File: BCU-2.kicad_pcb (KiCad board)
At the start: 2 copper layers, 91.9 x 68 mm, 70 parts, among them J1 Conn_01x12_Male, J2 Conn_01x04_Male, J3 Screw_Terminal_01x04, J4 Screw_Terminal_01x04, Q1 2N7002, Q2 NTF6P02, Q3 2N7002, Q4 2N7002, Q5 NTF6P02, Q6 2N7002, U1 PCF8574, U2 INA219xID, U3 INA219xID, U4 HCPL-181, U5 HCPL-181, U6 HCPL-181, U7 HCPL-181, U8 HCPL-181, U9 HCPL-181

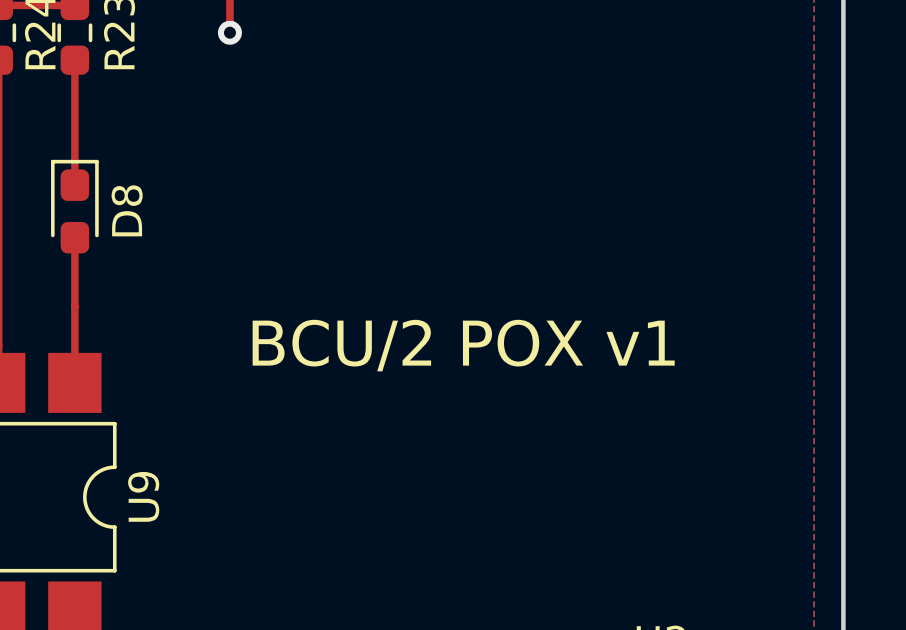
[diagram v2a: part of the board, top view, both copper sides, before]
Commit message: PCB: Update board name on silkscreen
Power-Opto eXtension Rev. 1.00

Signed-off-by: Geert Uytterhoeven <geert@linux-m68k.org>
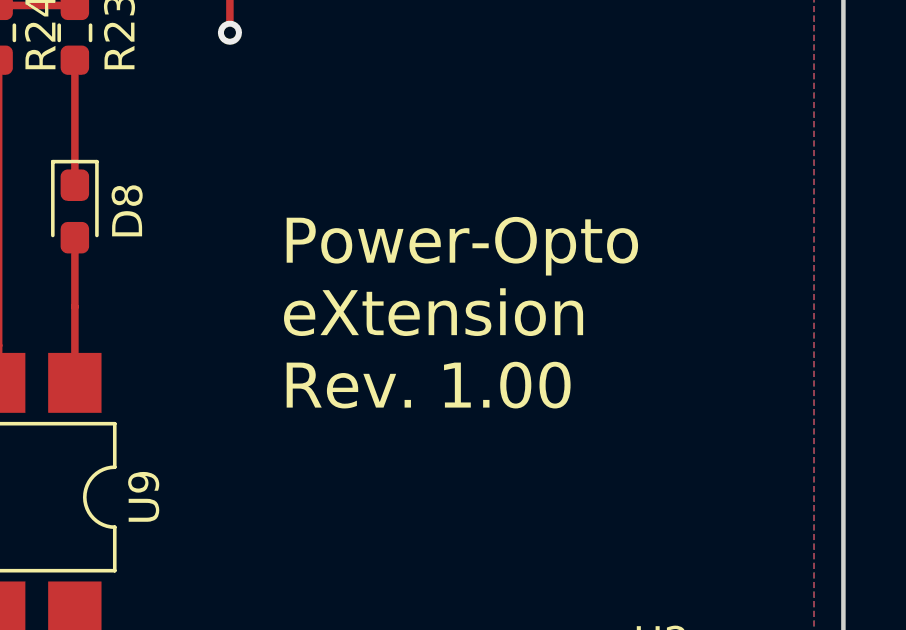
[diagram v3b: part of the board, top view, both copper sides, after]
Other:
- board text added: "Power-Opto eXtension Rev. 1.00"
- board text removed: "BCU/2 POX v1"
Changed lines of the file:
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@@
     (effects (font (size 1.2 1.2) (thickness 0.2)) (justify right))
   )
-  (gr_text "BCU/2 POX v1" (at 192.024 114.3) (layer "F.SilkS")
-    (effects (font (size 1.5 1.5) (thickness 0.3)))
+  (gr_text "Power-Opto\neXtension\nRev. 1.00" (at 185.928 113.284) (layer "F.SilkS")
+    (effects (font (size 1.5 1.5) (thickness 0.3)) (justify left))
   )
   (gr_text "- +" (at 161.29 130.937) (layer "F.SilkS")
